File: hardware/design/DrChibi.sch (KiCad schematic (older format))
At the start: 24 parts, among them P1 CONN_02X05, P2 PAD_SMD, P3 IN+, P4 IN-, X1 MINI-USB-SHIELD-32005-201

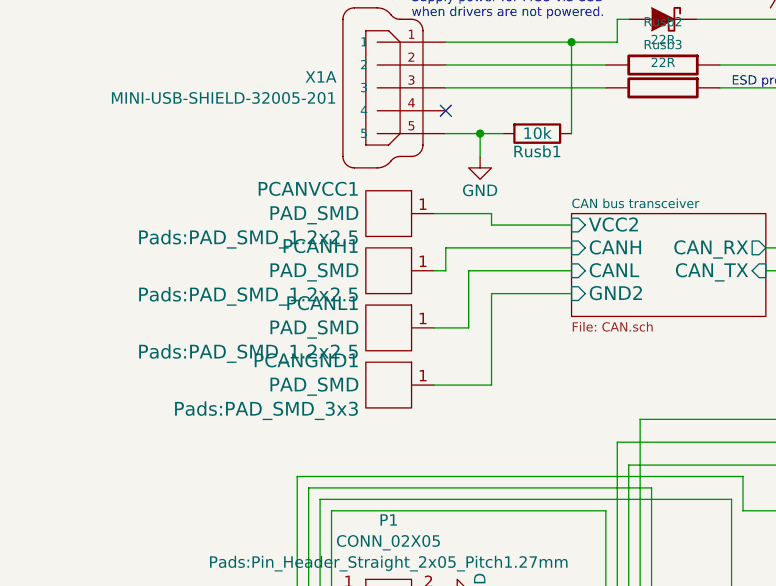
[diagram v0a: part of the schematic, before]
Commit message: Next step: connect GND and PWRGND.
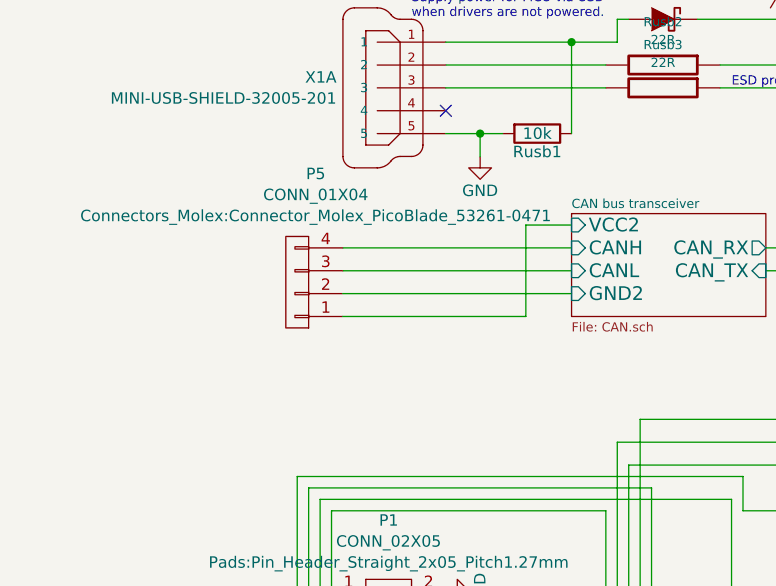
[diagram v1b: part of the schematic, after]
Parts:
- removed PCANGND1: PAD_SMD, Pads:PAD_SMD_3x3, symbol PAD_SMD
- removed PCANH1, PCANL1, PCANVCC1: PAD_SMD, Pads:PAD_SMD_1.2x2.5, symbol PAD_SMD
- added P5: CONN_01X04, Connectors_Molex:Connector_Molex_PicoBlade_53261-0471, symbol CONN_01X04
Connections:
- net CAN bus transceiver/CANH: now also P5.4 (P4)
- net CAN bus transceiver/CANL: now also P5.3 (P3)
- net CAN bus transceiver/GND2: now also P5.2 (P2)
- net CAN bus transceiver/VCC2: now also P5.1 (P1)

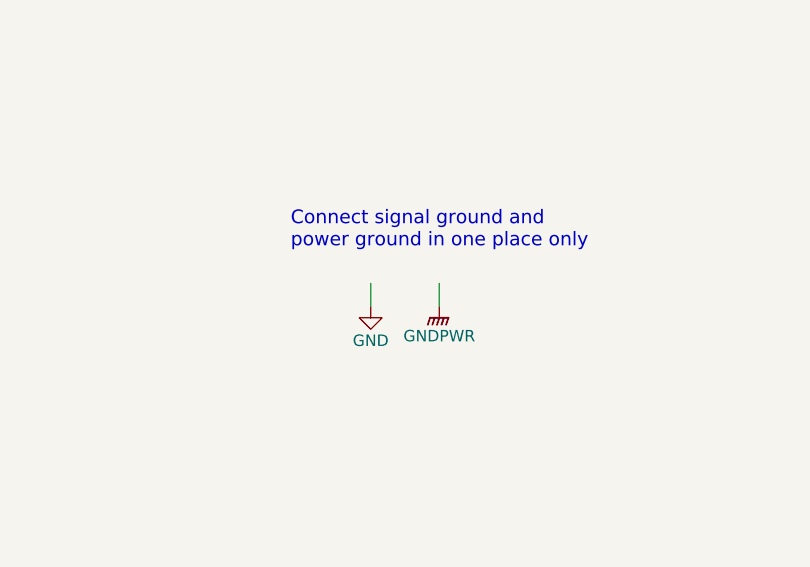
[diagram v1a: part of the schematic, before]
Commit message: GND and PWRGND connected.
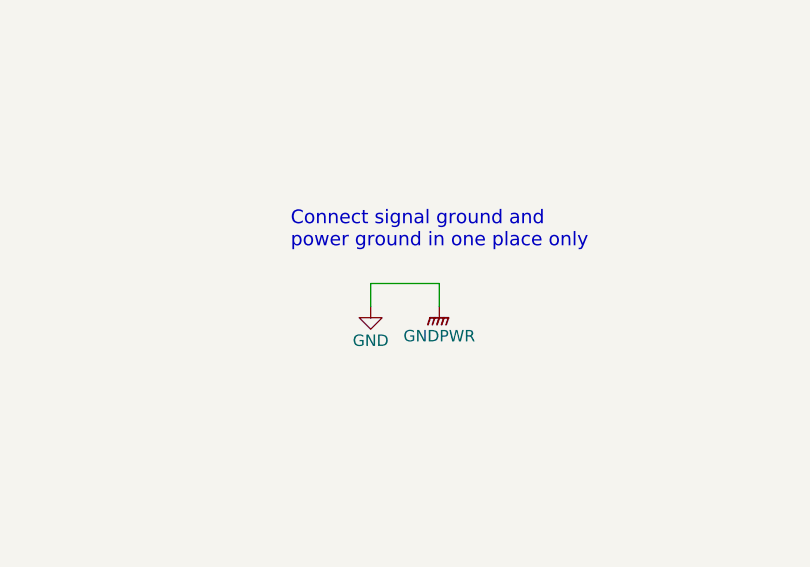
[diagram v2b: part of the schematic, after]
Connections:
- net GNDPWR is gone; now on net GND: P4.1
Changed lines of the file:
@@
 F47 "PWMF" O R 5700 5600 60
 $EndSheet
+Wire Wire Line
+	9450 5800 9750 5800
 $EndSCHEMATC

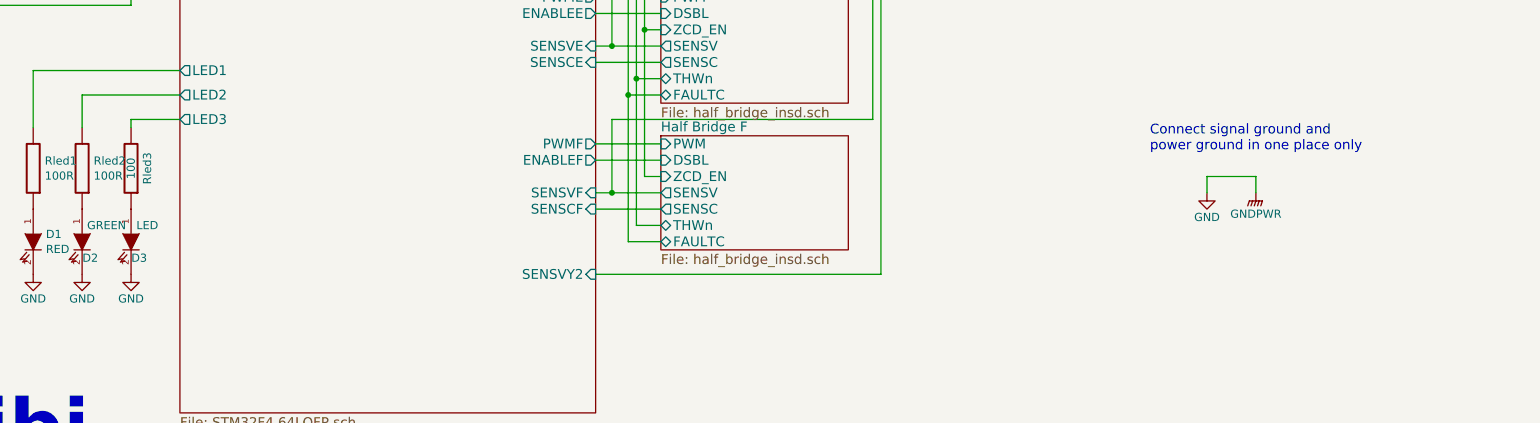
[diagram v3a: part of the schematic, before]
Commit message: Removed LED3 to gain some space for the 5V voltage regulator
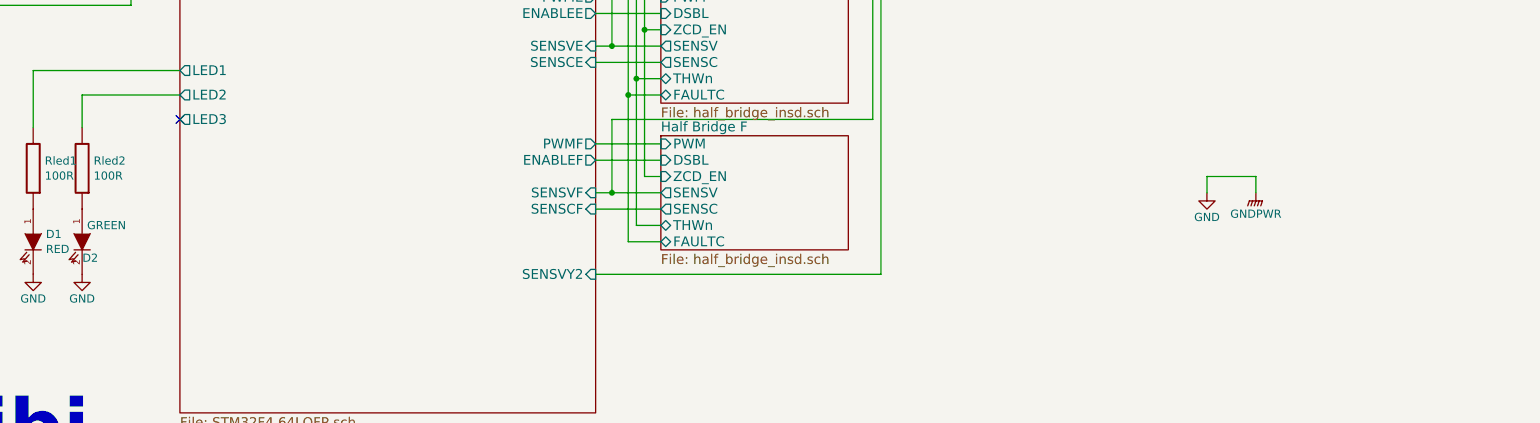
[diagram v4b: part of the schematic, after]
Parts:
- removed D3: LED, LEDs:LED_0603, symbol LED-RESCUE-BLDC_4
- removed Rled3: 100, Resistors_SMD:R_0603, symbol R-RESCUE-BLDC_4
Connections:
- no-connect marks 1 -> 2
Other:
- note removed: "Connect signal ground and\npower ground in one place only"
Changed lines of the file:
@@
 	0    1    1    0
 $EndComp
-$Comp
-L LED-RESCUE-BLDC_4 D3
-U 1 1 53FC6A60
-P 2850 6200
-F 0 "D3" V 2950 6250 50  0000 C CNN
-F 1 "LED" V 2750 6300 50  0000 C CNN
-F 2 "LEDs:LED_0603" H 2850 6200 60  0001 C CNN
-F 3 "" H 2850 6200 60  0001 C CNN
-	1    2850 6200
-	0    1    1    0
-$EndComp
-$Comp
-L R-RESCUE-BLDC_4 Rled3
-U 1 1 53FC6A67
-P 2850 5750
-F 0 "Rled3" V 2750 5750 50  0000 C CNN
-F 1 "100" V 2850 5750 50  0000 C CNN
-F 2 "Resistors_SMD:R_0603" H 2850 5750 60  0001 C CNN
-F 3 "" H 2850 5750 60  0001 C CNN
-	1    2850 5750
-	-1   0    0    1
-$EndComp
 $Bitmap
 Pos 9650 6250
@@
 EndData
 $EndBitmap
-Text Notes 9100 5650 0    60   ~ 0
-Connect signal ground and\npower ground in one place only
 $Sheet
 S 6100 950  1150 700
@@
 $Comp
 L GND #PWR05
-U 1 1 55E52B03
-P 2850 6400
-F 0 "#PWR05" H 2850 6150 50  0001 C CNN
-F 1 "GND" H 2850 6250 50  0000 C CNN
-F 2 "" H 2850 6400 60  0000 C CNN
-F 3 "" H 2850 6400 60  0000 C CNN
-	1    2850 6400
-	1    0    0    -1
-$EndComp
-$Comp
-L GND #PWR06
 U 1 1 55E58E48
 P 1600 1350
-F 0 "#PWR06" H 1600 1100 50  0001 C CNN
+F 0 "#PWR05" H 1600 1100 50  0001 C CNN
 F 1 "GND" H 1600 1200 50  0000 C CNN
 F 2 "" H 1600 1350 60  0000 C CNN
@@
 $EndComp
 $Comp
-L GND #PWR07
+L GND #PWR06
 U 1 1 55E592AD
 P 1500 2300
-F 0 "#PWR07" H 1500 2050 50  0001 C CNN
+F 0 "#PWR06" H 1500 2050 50  0001 C CNN
 F 1 "GND" H 1500 2150 50  0000 C CNN
 F 2 "" H 1500 2300 60  0000 C CNN
@@
 $EndComp
 $Comp
-L GND #PWR08
+L GND #PWR07
 U 1 1 55E5EC55
 P 1350 4200
-F 0 "#PWR08" H 1350 3950 50  0001 C CNN
+F 0 "#PWR07" H 1350 3950 50  0001 C CNN
 F 1 "GND" H 1350 4050 50  0000 C CNN
 F 2 "" H 1350 4200 60  0000 C CNN
@@
 $EndComp
 $Comp
-L GNDPWR #PWR09
+L GNDPWR #PWR08
 U 1 1 55E81E9B
 P 9400 2850
-F 0 "#PWR09" H 9400 2650 50  0001 C CNN
+F 0 "#PWR08" H 9400 2650 50  0001 C CNN
 F 1 "GNDPWR" H 9400 2720 50  0000 C CNN
 F 2 "" H 9400 2800 60  0000 C CNN
@@
 Goes to footprint
 $Comp
-L +24V #PWR010
+L +24V #PWR09
 U 1 1 56A6C8A8
 P 9400 2550
-F 0 "#PWR010" H 9400 2400 50  0001 C CNN
+F 0 "#PWR09" H 9400 2400 50  0001 C CNN
 F 1 "+24V" H 9418 2724 50  0000 C CNN
 F 2 "" H 9400 2550 50  0000 C CNN
@@
 $EndComp
 $Comp
-L +24V #PWR011
+L +24V #PWR010
 U 1 1 56A9BA22
 P 1550 1000
-F 0 "#PWR011" H 1550 850 50  0001 C CNN
+F 0 "#PWR010" H 1550 850 50  0001 C CNN
 F 1 "+24V" H 1568 1174 50  0000 C CNN
 F 2 "" H 1550 1000 50  0000 C CNN
@@
 $EndComp
 $Comp
-L +5V #PWR012
+L +5V #PWR011
 U 1 1 56AA4E2C
 P 2800 1700
-F 0 "#PWR012" H 2800 1550 50  0001 C CNN
+F 0 "#PWR011" H 2800 1550 50  0001 C CNN
 F 1 "+5V" H 2818 1874 50  0000 C CNN
 F 2 "" H 2800 1700 50  0000 C CNN
@@
 	5900 1600 6100 1600
 Wire Wire Line
-	2850 5500 2850 5450
-Wire Wire Line
-	2850 5450 3150 5450
-Wire Wire Line
 	2550 5500 2550 5300
 Wire Wire Line
@@
 Wire Wire Line
 	9450 5800 9750 5800
+NoConn ~ 3150 5450
 $EndSCHEMATC

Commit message: Do DRC check!
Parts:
- D1, D2: footprint LEDs:LED_0603 -> LEDs:LED_0402
- Rled1, Rled2: footprint Resistors_SMD:R_0603 -> Resistors_SMD:R_0402
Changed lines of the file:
@@
 F 0 "Rled1" H 2179 5704 50  0000 R CNN
 F 1 "100R" H 2179 5796 50  0000 R CNN
-F 2 "Resistors_SMD:R_0603" H 2250 5750 60  0001 C CNN
+F 2 "Resistors_SMD:R_0402" H 2250 5750 60  0001 C CNN
 F 3 "" H 2250 5750 60  0001 C CNN
 	1    2250 5750
@@
 F 0 "D1" V 2204 6278 50  0000 L CNN
 F 1 "RED" V 2296 6278 50  0000 L CNN
-F 2 "LEDs:LED_0603" H 2250 6200 60  0001 C CNN
+F 2 "LEDs:LED_0402" H 2250 6200 60  0001 C CNN
 F 3 "" H 2250 6200 60  0001 C CNN
 	1    2250 6200
@@
 F 0 "Rled2" H 2479 5704 50  0000 R CNN
 F 1 "100R" H 2479 5796 50  0000 R CNN
-F 2 "Resistors_SMD:R_0603" H 2550 5750 60  0001 C CNN
+F 2 "Resistors_SMD:R_0402" H 2550 5750 60  0001 C CNN
 F 3 "" H 2550 5750 60  0001 C CNN
 	1    2550 5750
@@
 F 0 "D2" V 2650 6250 50  0000 C CNN
 F 1 "GREEN" V 2450 6350 50  0000 C CNN
-F 2 "LEDs:LED_0603" H 2550 6200 60  0001 C CNN
+F 2 "LEDs:LED_0402" H 2550 6200 60  0001 C CNN
 F 3 "" H 2550 6200 60  0001 C CNN
 	1    2550 6200
